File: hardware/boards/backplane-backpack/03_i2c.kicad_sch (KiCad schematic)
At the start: 33 parts, among them J3 I2C CH0 (TBD), J4 I2C CH1 (TBD), J5 I2C CH2 (TBD), J6 I2C CH3 (TBD), J7 I2C CH4 (TBD), J8 I2C CH5 (TBD), U2 TCA9548APWR

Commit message: chore: checkpoint workspace changes
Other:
- company: (none) -> Karl Quinsland
- title: I2C Multiplexer and Ports -> Backplane Backpack

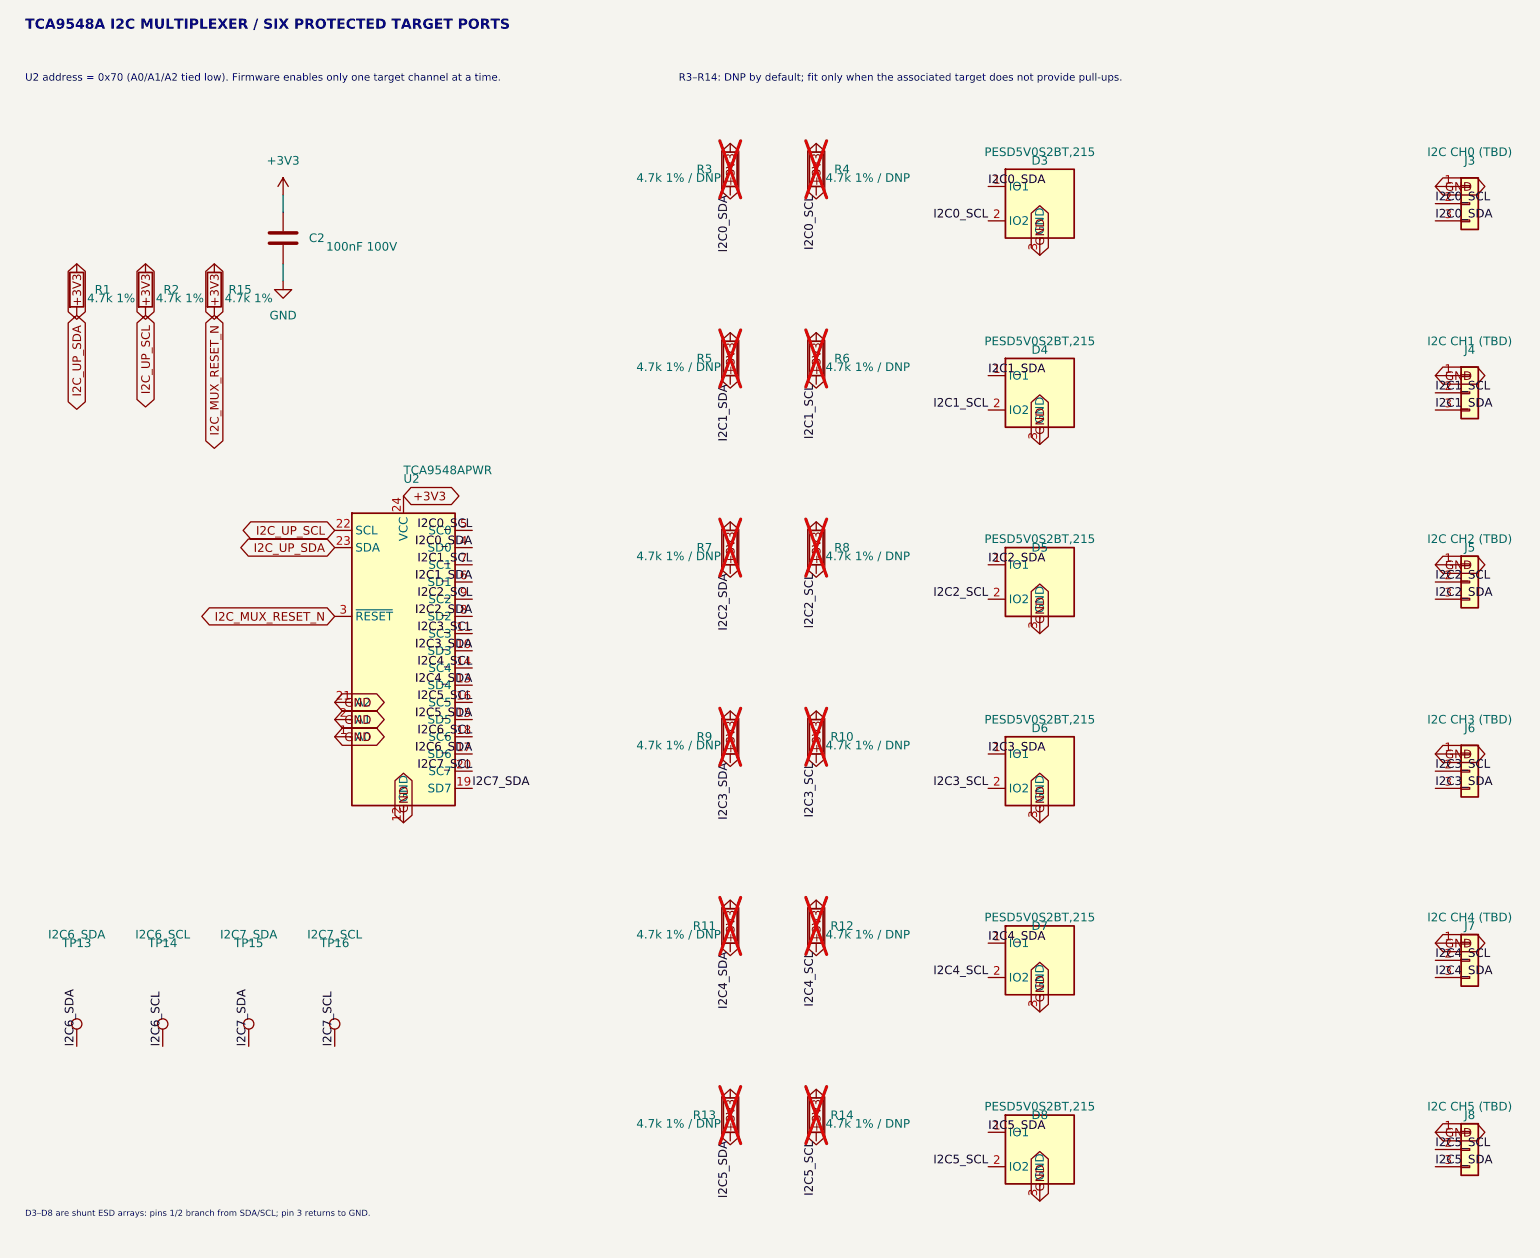
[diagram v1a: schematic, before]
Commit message: fix: normalize power symbols and connector grounds
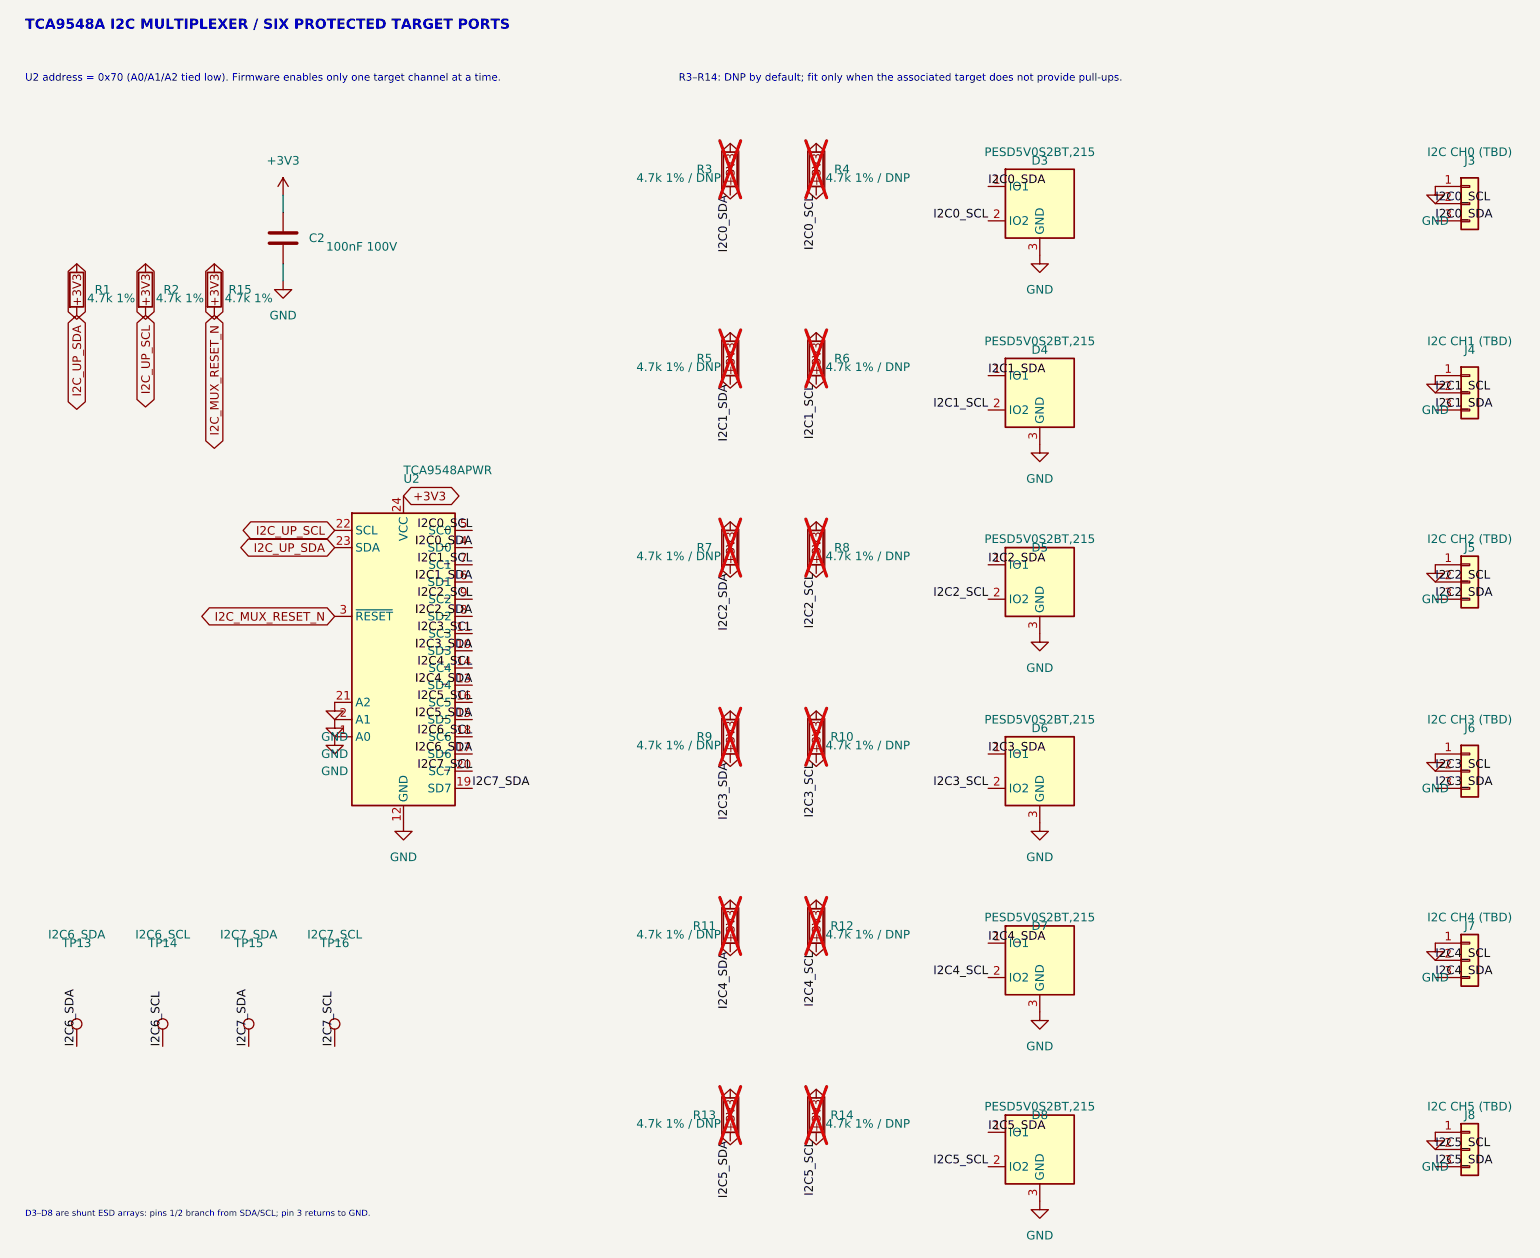
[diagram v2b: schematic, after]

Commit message: fix: standardize +3V3 power symbols
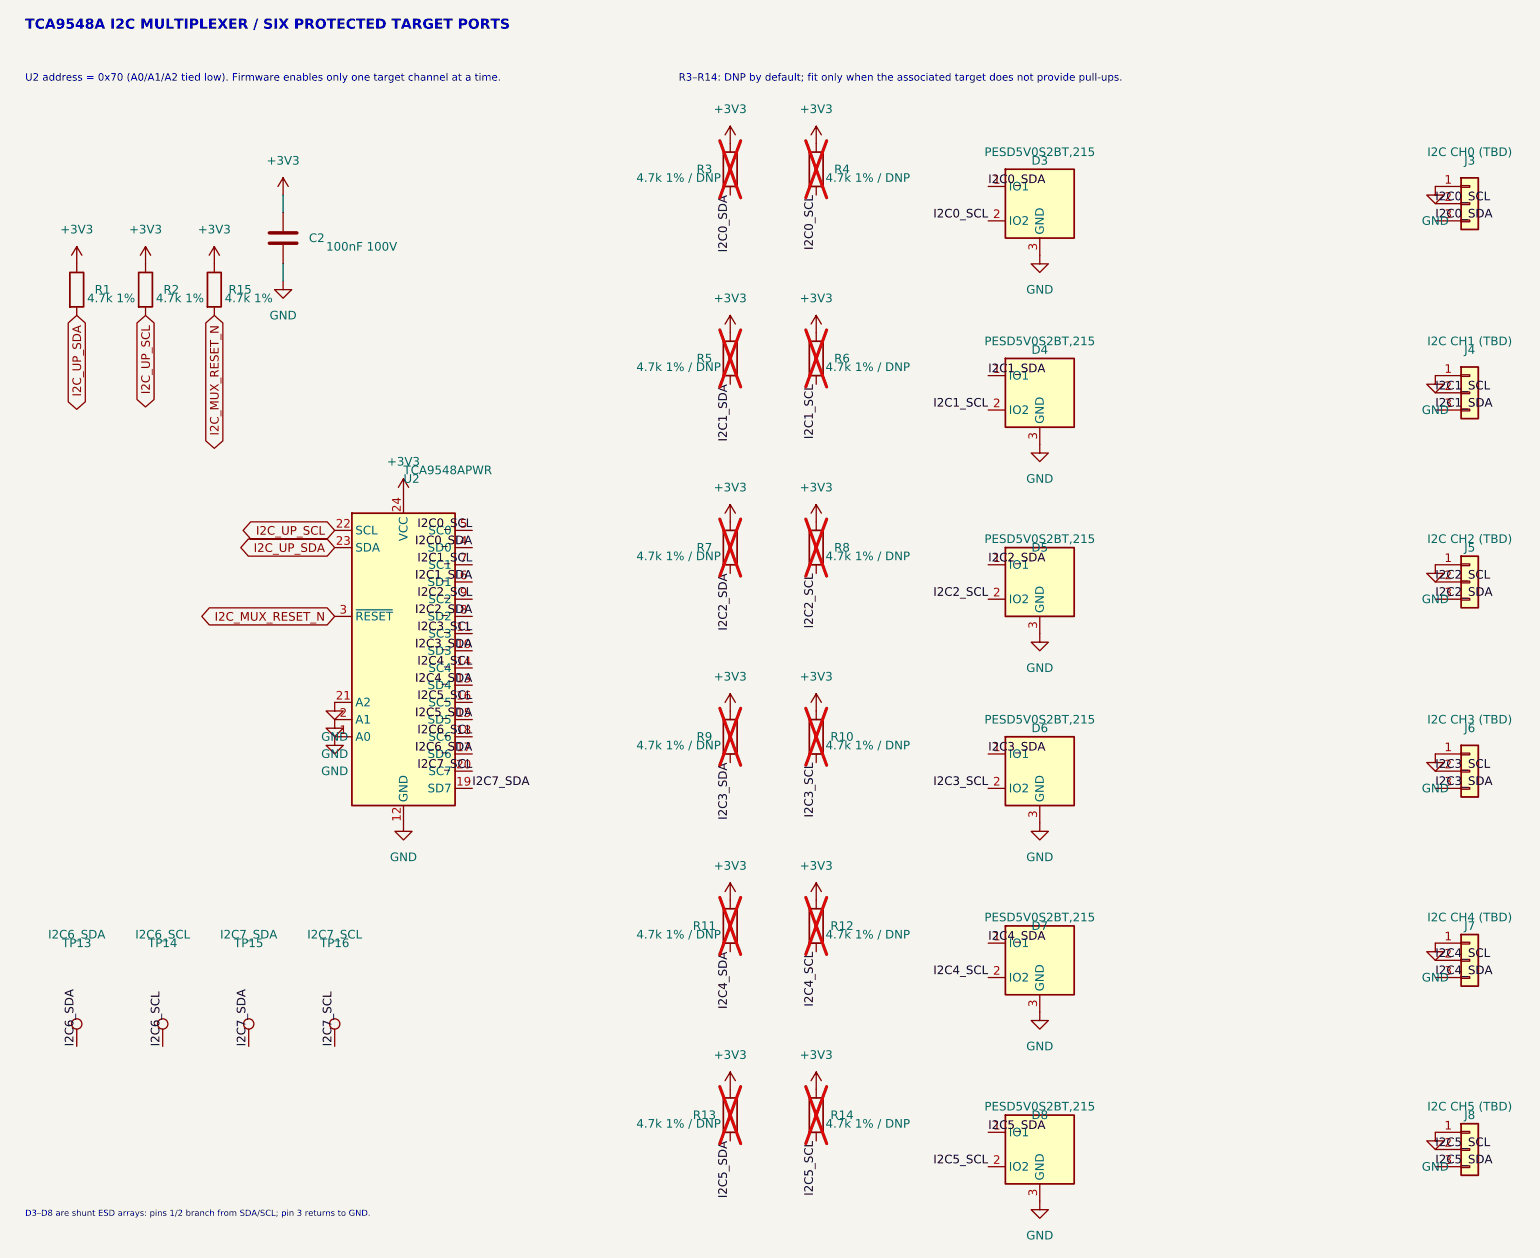
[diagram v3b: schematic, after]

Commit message: chore: checkpoint workspace changes
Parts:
- removed D3: PESD5V0S2BT,215, Package_TO_SOT_SMD:SOT-23, symbol backplane-backpack:PESD_Dual_SOT23
- removed R3, R4: 4.7k 1% / DNP, Resistor_SMD:R_0603_1608Metric, symbol Device:R
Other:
- note removed: "R3–R14: DNP by default; fit only when the associated target does not provide pull-ups."

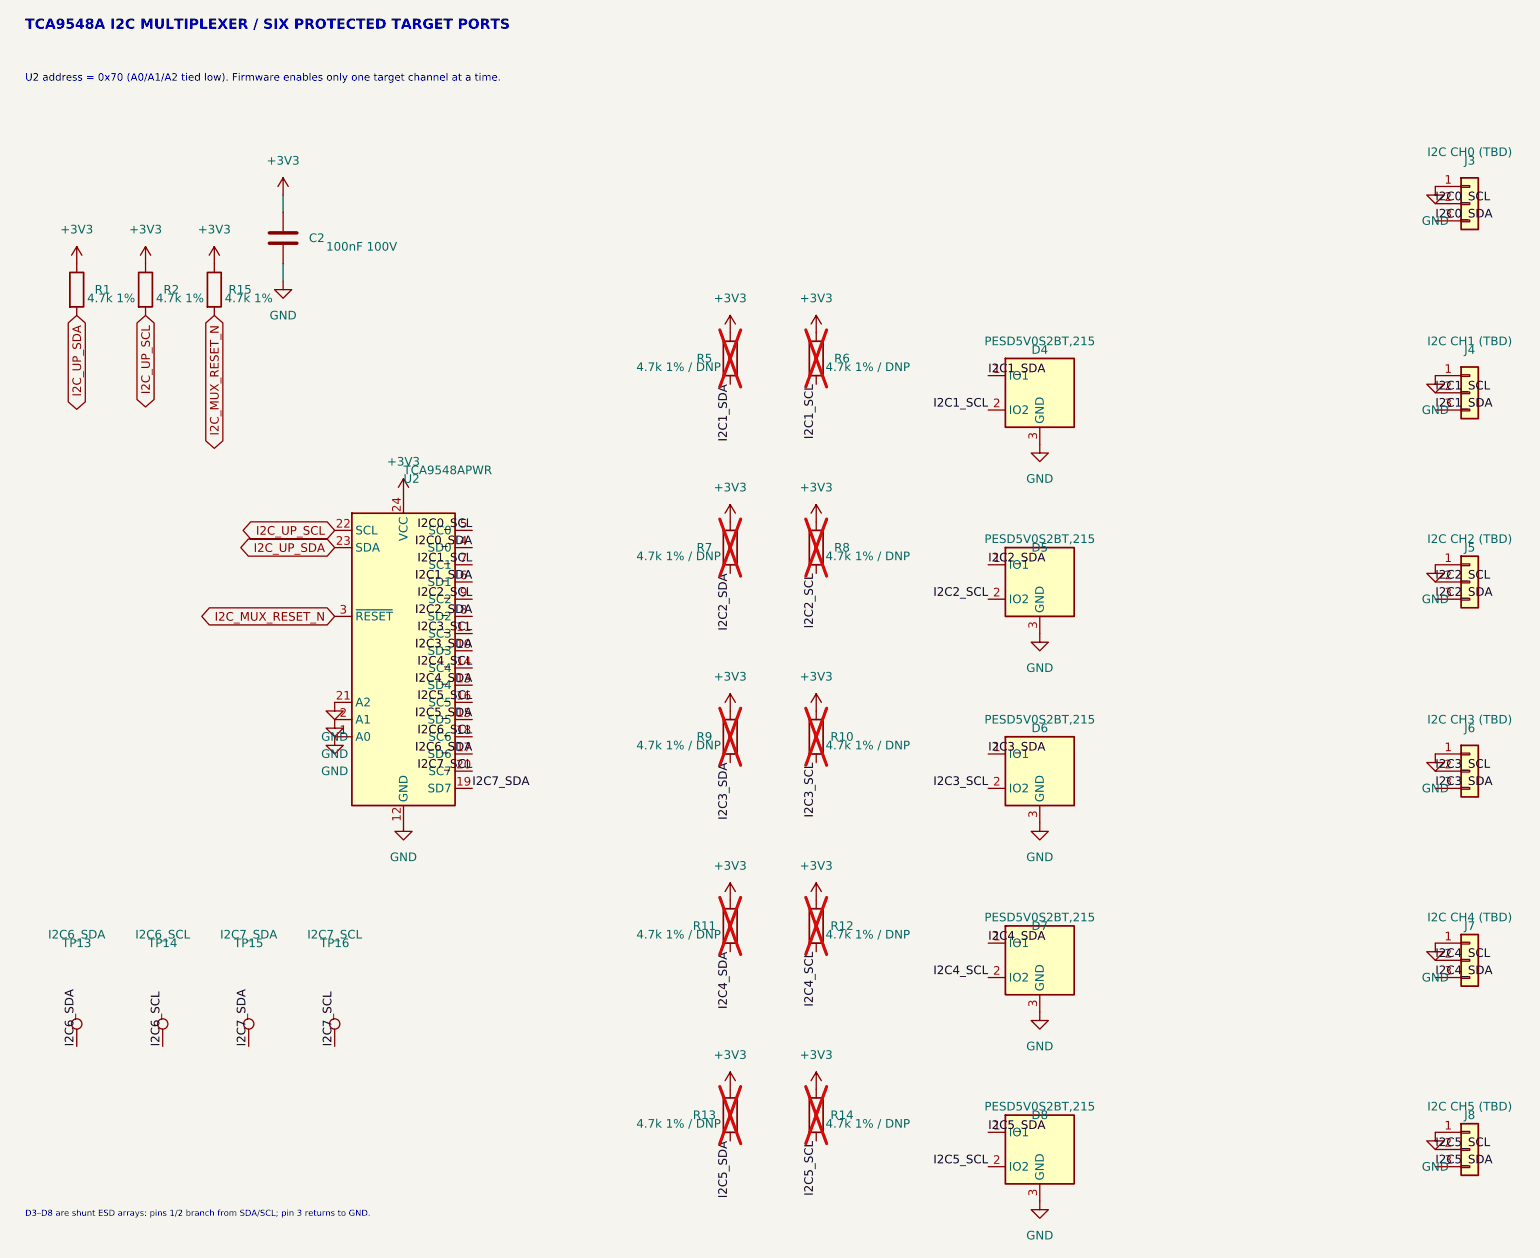
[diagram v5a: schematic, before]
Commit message: refactor: move slot I2C protection to backplane
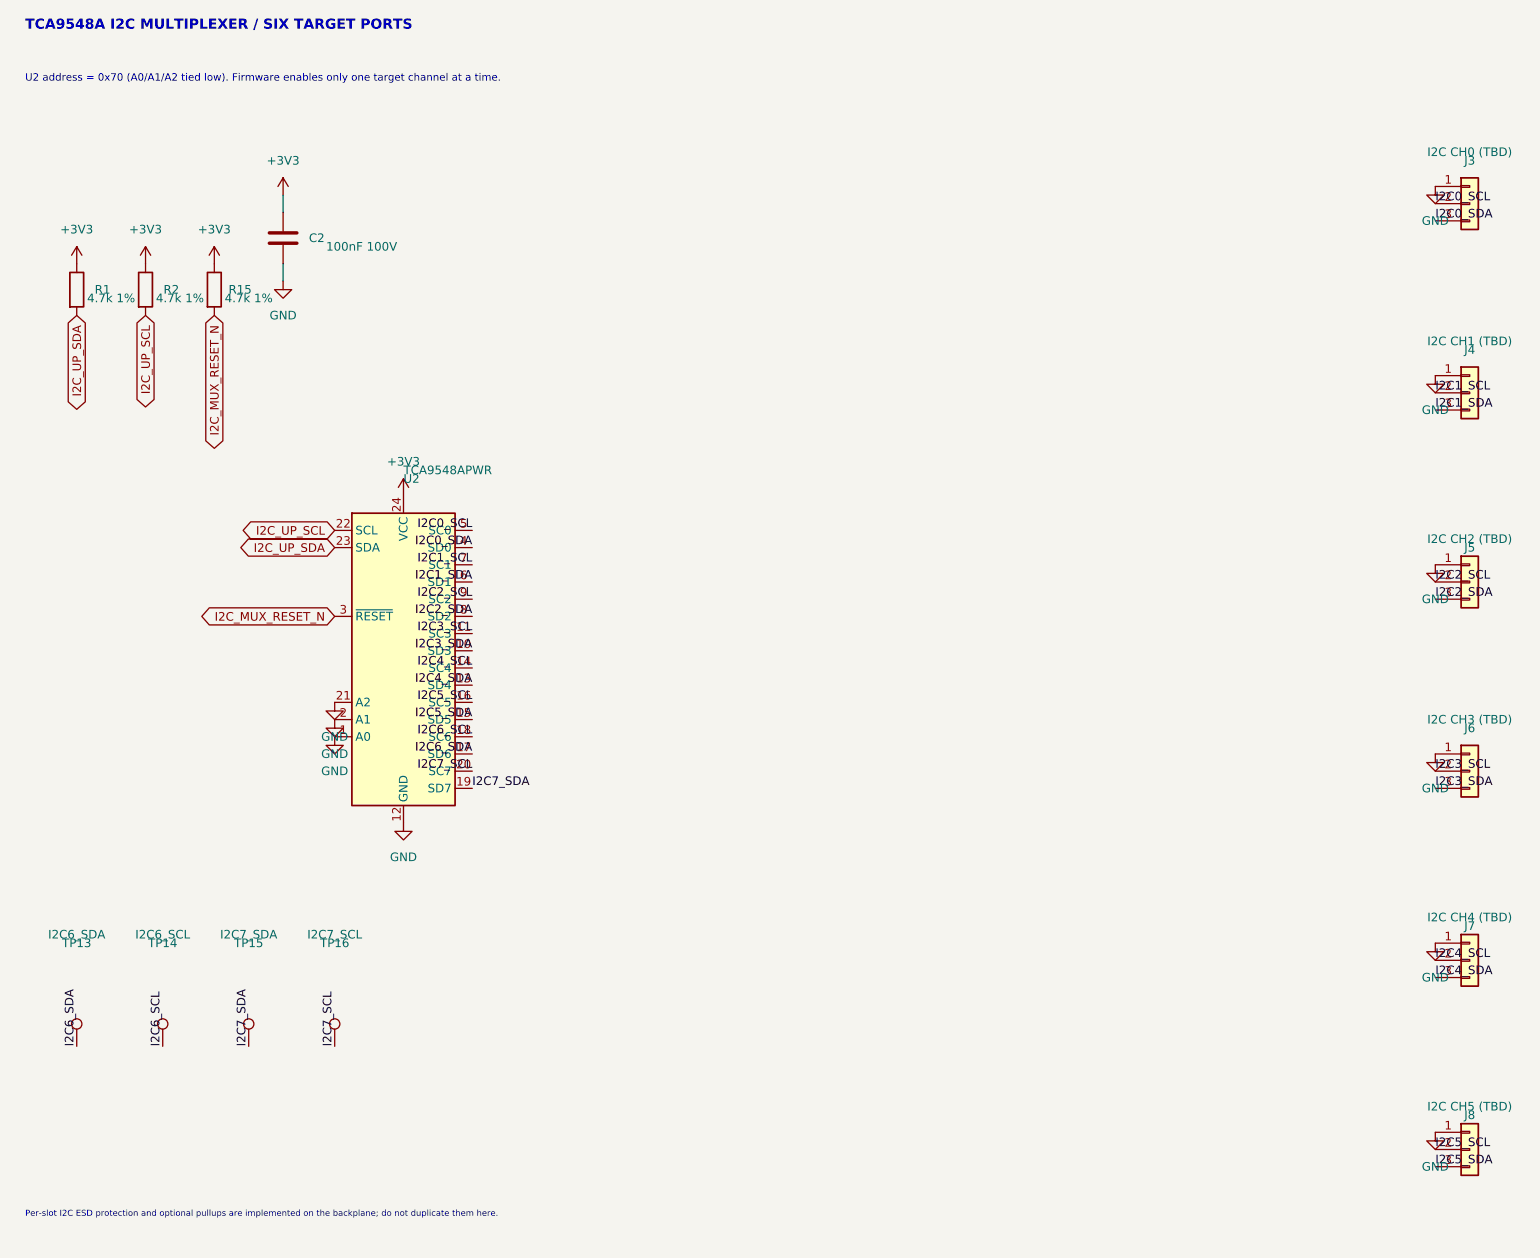
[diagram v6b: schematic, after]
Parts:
- removed D4, D5, D6, D7, D8: PESD5V0S2BT,215, Package_TO_SOT_SMD:SOT-23, symbol backplane-backpack:PESD_Dual_SOT23
- removed R10, R11, R12, R13, R14, R5, R6, R7, R8, R9: 4.7k 1% / DNP, Resistor_SMD:R_0603_1608Metric, symbol Device:R
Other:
- note added: "Per-slot I2C ESD protection and optional pullups are implemented on the backplane; do not duplicate them here."
- note added: "TCA9548A I2C MULTIPLEXER / SIX TARGET PORTS"
- note removed: "D3–D8 are shunt ESD arrays: pins 1/2 branch from SDA/SCL; pin 3 returns to GND."
- note removed: "TCA9548A I2C MULTIPLEXER / SIX PROTECTED TARGET PORTS"
